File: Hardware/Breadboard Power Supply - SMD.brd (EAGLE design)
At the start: 54.6 x 16.5 mm, 29 parts, among them J1 POWER_JACKSMD, U1 V_REG_317SMD

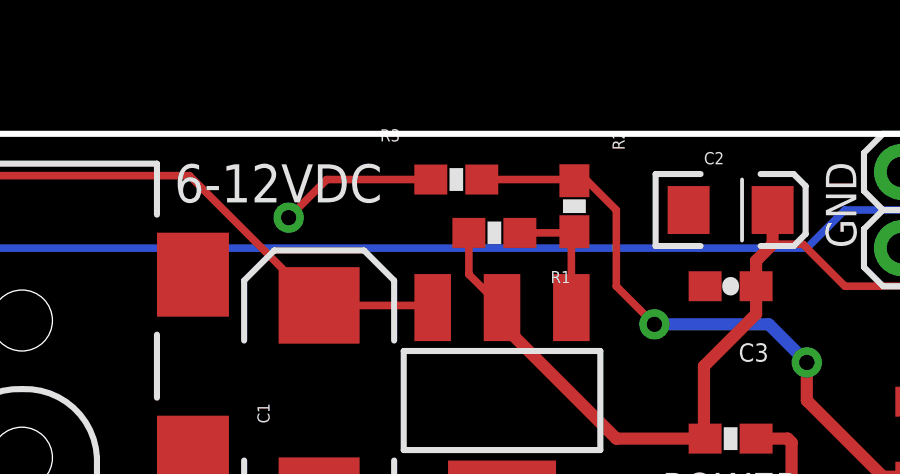
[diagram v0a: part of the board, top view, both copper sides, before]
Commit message: fixed board name
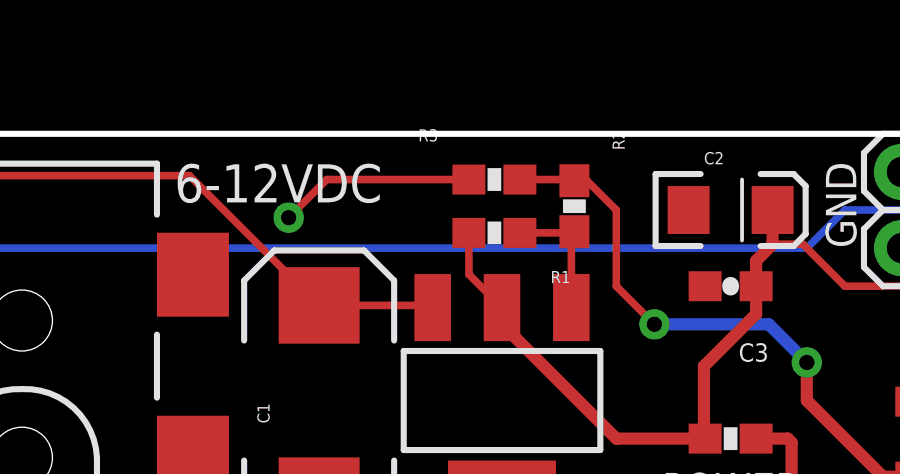
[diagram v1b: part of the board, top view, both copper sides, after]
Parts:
- moved U$2 3.81 mm to (37.1, 10.3)
- moved R3 1.27 mm to (34.0, 15.0)
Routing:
- net N$4: track 20.7 -> 19.4 mm
- net GND: track 19.5 -> 20.8 mm
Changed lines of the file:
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@@
 <layer number="47" name="Measures" color="7" fill="1" visible="no" active="yes"/>
 <layer number="48" name="Document" color="7" fill="1" visible="no" active="yes"/>
-<layer number="49" name="Reference" color="7" fill="1" visible="yes" active="yes"/>
+<layer number="49" name="Reference" color="7" fill="1" visible="no" active="yes"/>
 <layer number="50" name="dxf" color="7" fill="1" visible="no" active="yes"/>
 <layer number="51" name="tDocu" color="6" fill="1" visible="yes" active="yes"/>
@@
 <text x="-76.2" y="0" size="1.778" layer="27" font="vector" ratio="15">N. Seidle</text>
 <text x="-96.52" y="-2.54" size="1.778" layer="27" font="vector" ratio="15">Revised By: T Talmage</text>
-<text x="49.657" y="4.572" size="1.778" layer="22" font="vector" ratio="15" rot="MR0">Breadboard Power Supply Stick </text>
-<text x="33.147" y="2.413" size="1.778" layer="22" font="vector" ratio="15" rot="MR0">3.3v-5v</text>
+<text x="49.657" y="8.382" size="1.778" layer="22" font="vector" ratio="15" rot="MR0">Breadboard Power Supply Stick </text>
+<text x="34.417" y="6.223" size="1.778" layer="22" font="vector" ratio="15" rot="MR0">3.3v-5v</text>
 </plain>
 <attributes>
@@
 <attribute name="VALUE" x="49.657" y="5.588" size="0.4064" layer="27" rot="R90"/>
 </element>
-<element name="R3" library="SparkFun" package="0603-RES" value="330" x="32.766" y="14.986" smashed="yes">
-<attribute name="NAME" x="30.226" y="16.256" size="0.4064" layer="25"/>
+<element name="R3" library="SparkFun" package="0603-RES" value="330" x="34.036" y="14.986" smashed="yes">
+<attribute name="NAME" x="31.496" y="16.256" size="0.4064" layer="25"/>
 </element>
 <element name="S1" library="SparkFun" package="AYZ0202" value="On/Off" x="3.81" y="5.08" rot="R270"/>
-<element name="U$2" library="SparkFun" package="SFE-NEW-WEBLOGO" value="LOGO-SFENEW" x="37.084" y="6.477" rot="MR0"/>
+<element name="U$2" library="SparkFun" package="SFE-NEW-WEBLOGO" value="LOGO-SFENEW" x="37.084" y="10.287" rot="MR0"/>
 <element name="U$3" library="SparkFun" package="FIDUCIAL-1X2" value="FIDUCIAL1X2" x="8.89" y="1.27"/>
 <element name="U$4" library="SparkFun" package="FIDUCIAL-1X2" value="FIDUCIAL1X2" x="53.086" y="14.478"/>
@@
 <wire x1="35.56" y1="2.54" x2="30.104" y2="2.54" width="0.254" layer="1"/>
 <wire x1="30.104" y1="2.54" x2="28.194" y2="4.45" width="0.254" layer="1"/>
-<wire x1="31.916" y1="14.986" x2="28.448" y2="14.986" width="0.254" layer="1"/>
+<wire x1="33.186" y1="14.986" x2="28.448" y2="14.986" width="0.254" layer="1"/>
 <wire x1="28.448" y1="14.986" x2="27.178" y2="13.716" width="0.254" layer="1"/>
 </signal>
@@
 <wire x1="38.1" y1="13.97" x2="38.1" y2="11.43" width="0.254" layer="1"/>
 <wire x1="38.1" y1="11.43" x2="39.37" y2="10.16" width="0.254" layer="1"/>
-<wire x1="33.616" y1="14.986" x2="36.664" y2="14.986" width="0.254" layer="1"/>
+<wire x1="34.886" y1="14.986" x2="36.664" y2="14.986" width="0.254" layer="1"/>
 <wire x1="36.664" y1="14.986" x2="36.703" y2="14.947" width="0.254" layer="1"/>
 </signal>
